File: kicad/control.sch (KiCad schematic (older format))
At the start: 16 parts, among them SW5 SW_Push, U33 74LS00, U37 74LS161, U38 28C16, U39 74LS138, U40 74LS00, U41 28C16

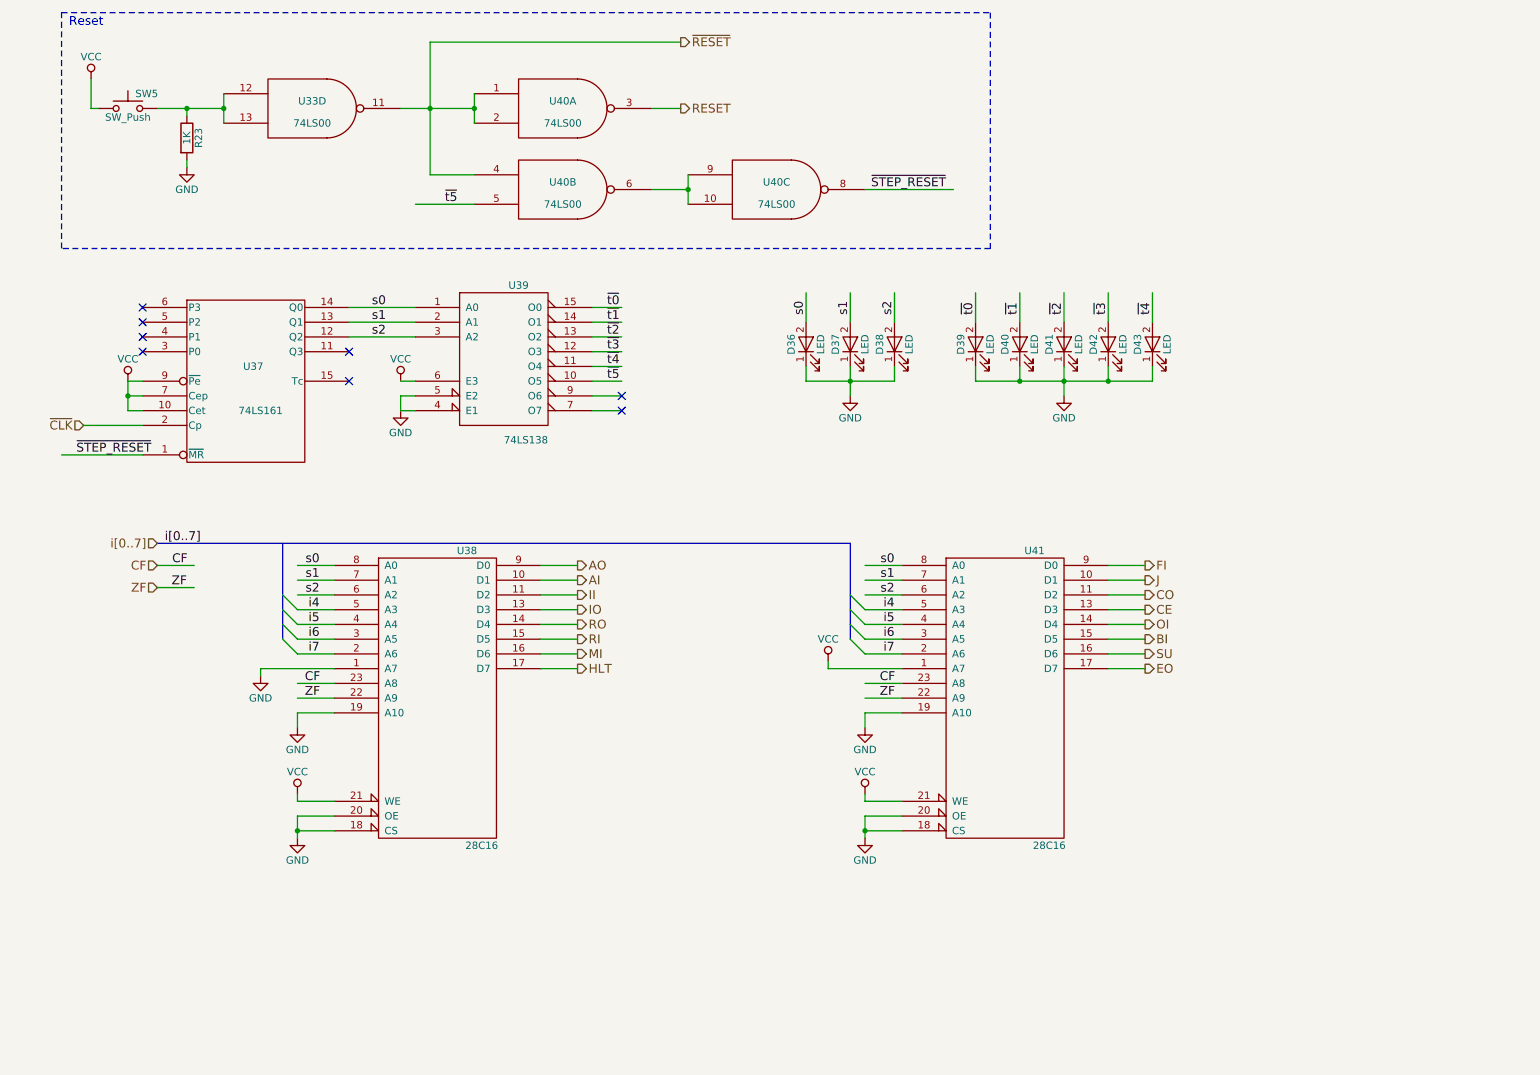
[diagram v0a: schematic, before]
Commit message: Update bugfix version to use updated kicad libraries
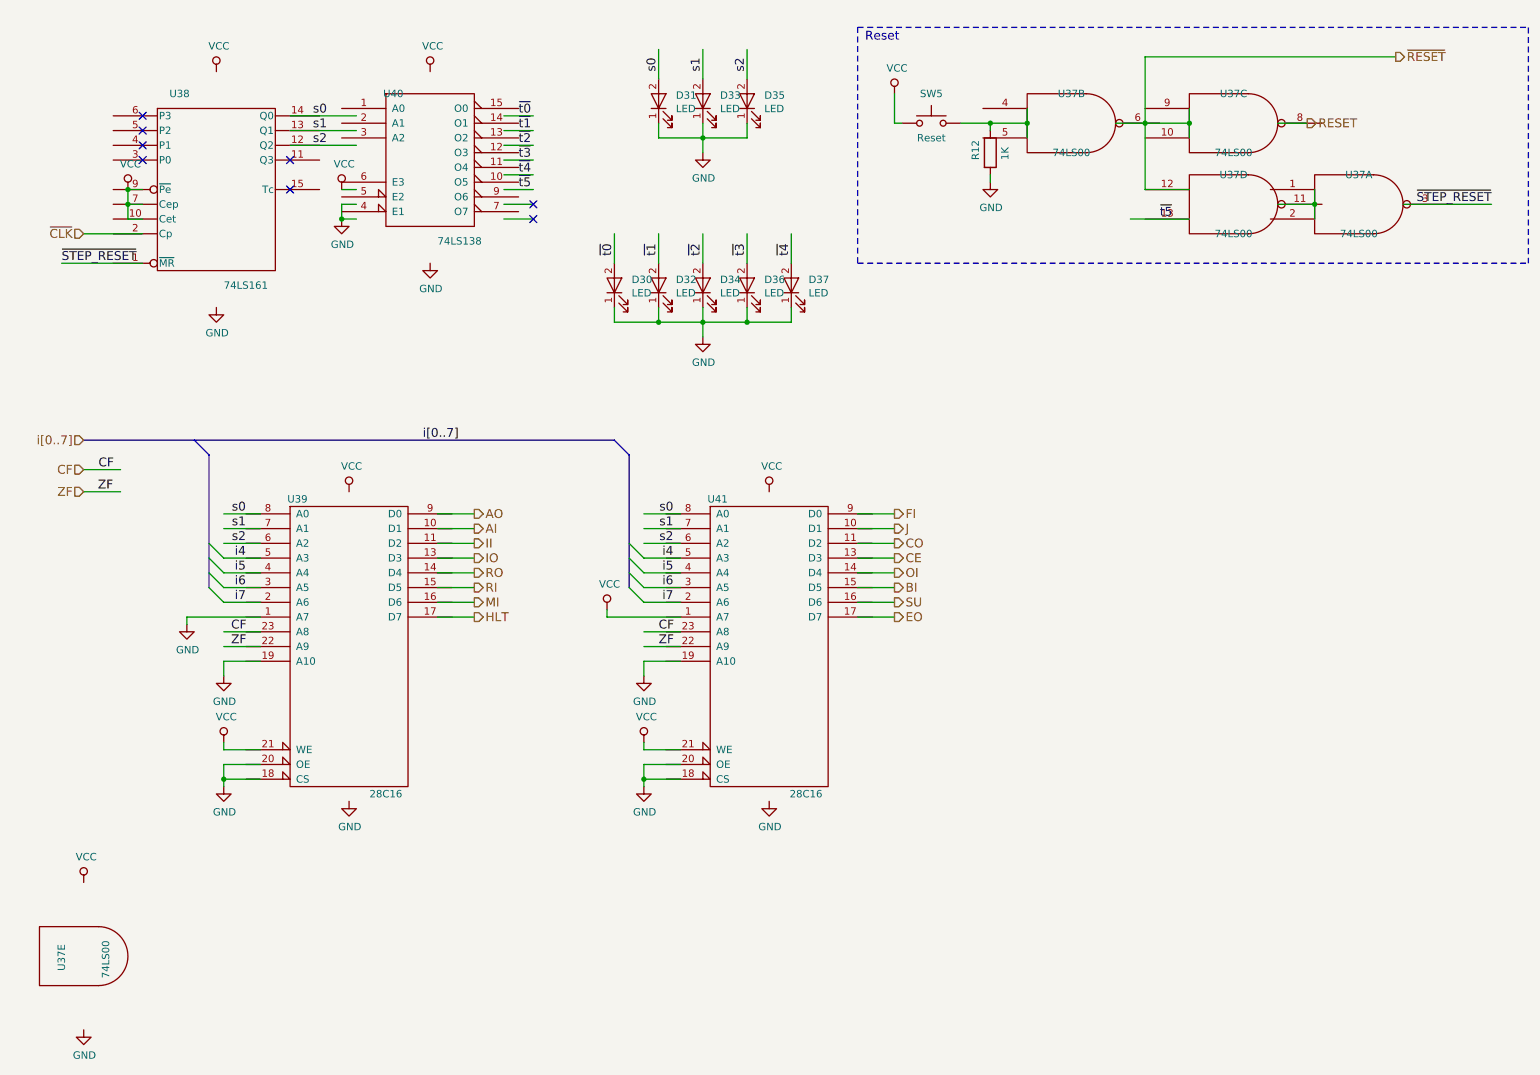
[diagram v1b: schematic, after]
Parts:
- removed D36, D37, D38, D39, D40, D41, D42, D43: LED, symbol LED
- removed R23: 1K, symbol R
- removed SW5: SW_Push, symbol SW_Push
- removed U33, U40: 74LS00, symbol 74LS00
- removed U37: 74LS161, Housings_DIP:DIP-16_W7.62mm_LongPads, symbol 74LS161
- removed U38, U41: 28C16, Housings_DIP:DIP-24_W15.24mm_LongPads, symbol 28C16
- removed U39: 74LS138, Housings_DIP:DIP-16_W7.62mm_LongPads, symbol 74LS138
- added D30, D31, D32, D33, D34, D35, D36, D37: LED, symbol Device:LED
- added R12: 1K, symbol Device:R
- added SW5: Reset, symbol Switch:SW_Push
- added U37: 74LS00, symbol 74xx:74LS00
- added U38: 74LS161, symbol 74xx:74LS161
- added U39, U41: 28C16, symbol sap-be:28C16
- added U40: 74LS138, symbol 74xx:74LS138
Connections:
- wire segments 109 -> 124

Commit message: update kicad project name
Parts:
- U39, U41: symbol sap-be:28C16 -> sap:28C16
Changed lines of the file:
@@
 $EndComp
 $Comp
-L sap-be:28C16 U39
+L sap:28C16 U39
 U 1 1 622FB85B
 P 3050 4900
@@
 $EndComp
 $Comp
-L sap-be:28C16 U41
+L sap:28C16 U41
 U 1 1 6230695B
 P 5900 4900
